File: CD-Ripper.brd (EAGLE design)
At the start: 100 x 80 mm, 35 parts, among them IC1 MEGA48/88/168-PU, IC2 5V, K1 351, K2 JS-M1-12V-5, K3 351, K4 JS-M1-12V-5, Q1 20MHz, X1 MOTOR1, X2 MOTOR2, X3 USBPTH, X4 STATUS1, X5 STATUS2

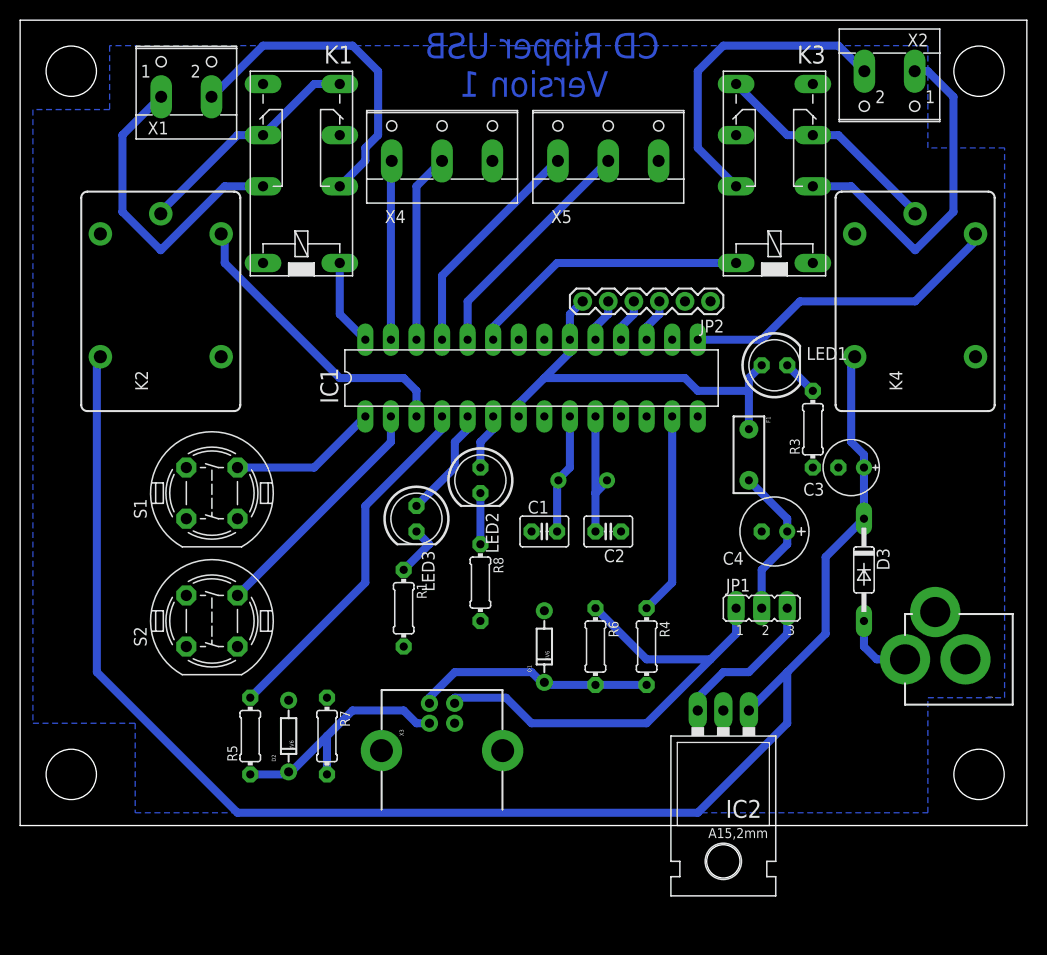
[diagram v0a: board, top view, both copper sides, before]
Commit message: Changed ICSP header.
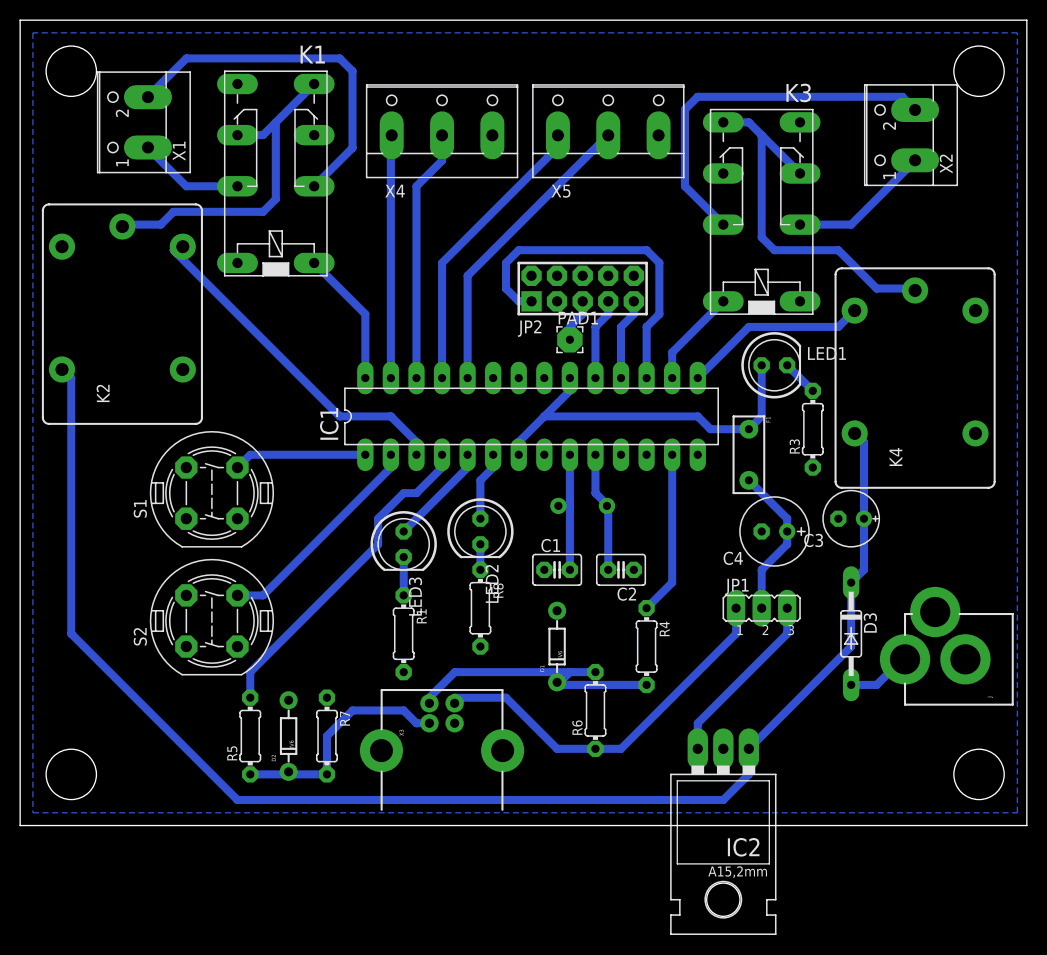
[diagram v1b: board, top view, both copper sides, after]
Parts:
- added PAD1: WIREPAD2,54/0,8, wirepad:2,54/0,8
- JP2: value (none) -> AVR-ISP-10; device SparkFun:1X06 -> avr-7:AVR-ISP-10
- moved JP2 12.8 mm to (55.9, 53.3), turned to 0 degrees
- moved K4 7.62 mm to (88.9, 44.5)
- moved D3 6.48 mm to (82.5, 19.1)
- moved X1 6.35 mm to (11.4, 69.8), turned to 90 degrees
- moved R6 6.35 mm to (57.1, 11.4), turned to 90 degrees
- moved X2 5.24 mm to (87.6, 68.6), turned to 90 degrees
- moved C3 5.08 mm to (82.5, 30.5)
- moved LED2 5.08 mm to (45.7, 29.2)
- moved C1 4.02 mm to (53.3, 25.4)
- moved K2 4.02 mm to (10.2, 50.8)
- moved C2 4.02 mm to (59.7, 25.4)
- moved K3 4.02 mm to (73.7, 55.9)
- moved IC1 3.81 mm to (50.8, 40.6)
- moved IC2 3.81 mm to (69.8, 3.81)
- moved LED3 2.84 mm to (38.1, 27.9)
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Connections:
- net N$11 renamed PC1
- removed net N$15: IC1.19, JP2.5
- removed net N$16: IC1.18, JP2.4
- removed net N$17: IC1.17, JP2.3
- new net MISO: IC1.18, JP2.9
- new net MOSI: IC1.17, JP2.1
- new net PD1: IC1.3, K2.2
- new net SCK: IC1.19, JP2.7
- net GND: now also JP2.10, JP2.3, JP2.4, JP2.6, JP2.8, K4.2; no longer JP2.1, K4.1
- net N$10: now also JP2.5, PAD1.1; no longer IC1.25, X5.1
- net PB1: now also K4.1; no longer K4.2
- net PB2: now also IC1.16; no longer IC1.23
- net PC2: now also IC1.25, X5.1; no longer IC1.26, X4.2
- net PC3: now also IC1.26, X4.2; no longer IC1.27, X4.1
- net PC4: now also IC1.27, X4.1; no longer IC1.28, K1.1
- net PC5: now also IC1.28, K1.1; no longer IC1.3, K2.2
- net VCC: no longer JP2.6
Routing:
- net PD1: track 0.00 -> 34.3 mm
- net MOSI: track 0.00 -> 33.9 mm
- net N$3: track 31.2 -> 10.5 mm
- net N$5: track 34.5 -> 14.1 mm
- net PB2: track 28.0 -> 9.72 mm
- net N$10: track 22.6 -> 4.34 mm
- net PC5: track 29.9 -> 13.5 mm
- net PC4: track 8.67 -> 24.1 mm
- net PB1: track 32.6 -> 18.4 mm
- net N$13: track 23.2 -> 37.4 mm
- net +12V: track 155.0 -> 140.9 mm
- net VBUS: track 49.3 -> 37.9 mm
- net N$12: track 23.2 -> 33.8 mm
- net PC2: track 18.9 -> 28.8 mm
- net SCK: track 0.00 -> 8.15 mm
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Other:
- board text removed: "CD Ripper USB"
- board text removed: "Version 1"
